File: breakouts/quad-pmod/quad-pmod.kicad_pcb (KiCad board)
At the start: 2 copper layers, 52.1 x 27.9 mm, 9 parts, among them J1 PMOD, J2 PMOD, J3 S7 Mini, J4 S7 Mini, J5 PWR, J6 PWR, J7 PMOD, J8 PMOD

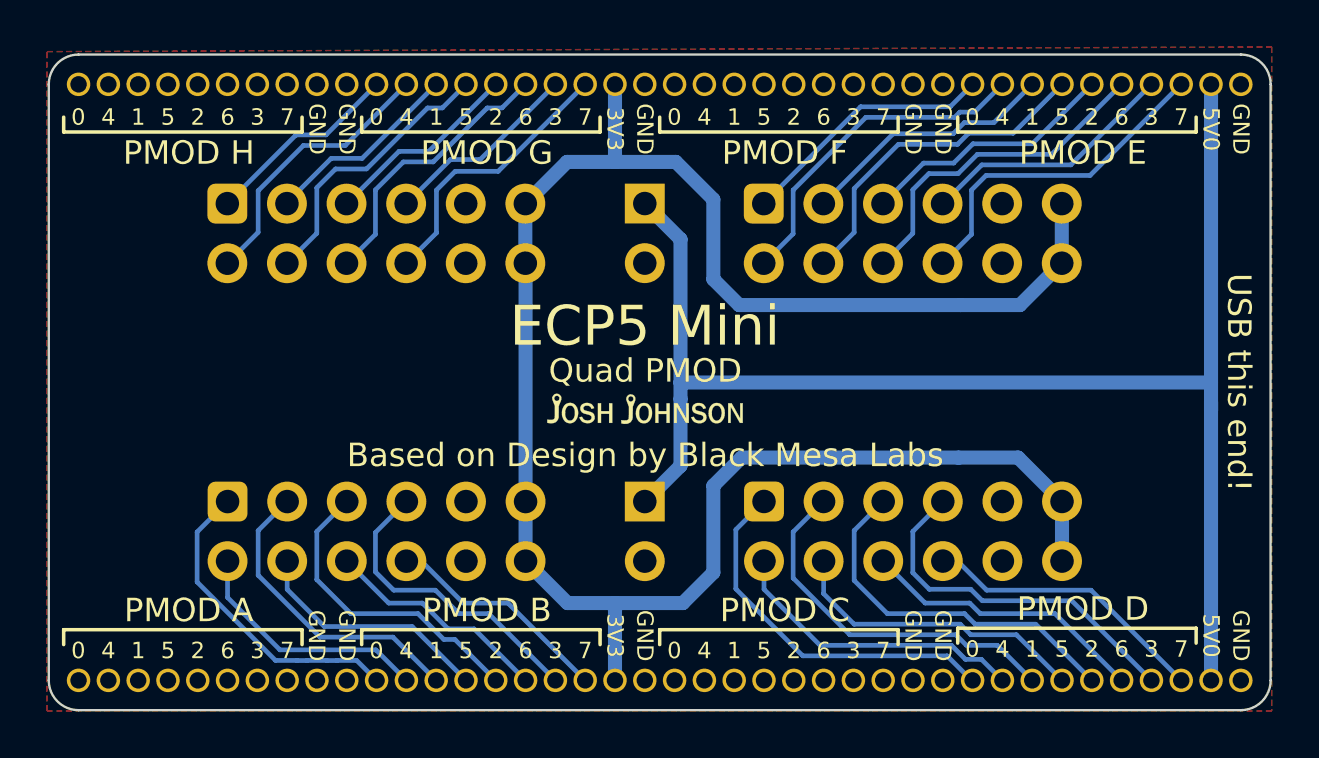
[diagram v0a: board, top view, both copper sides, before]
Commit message: update silk to clear connectors
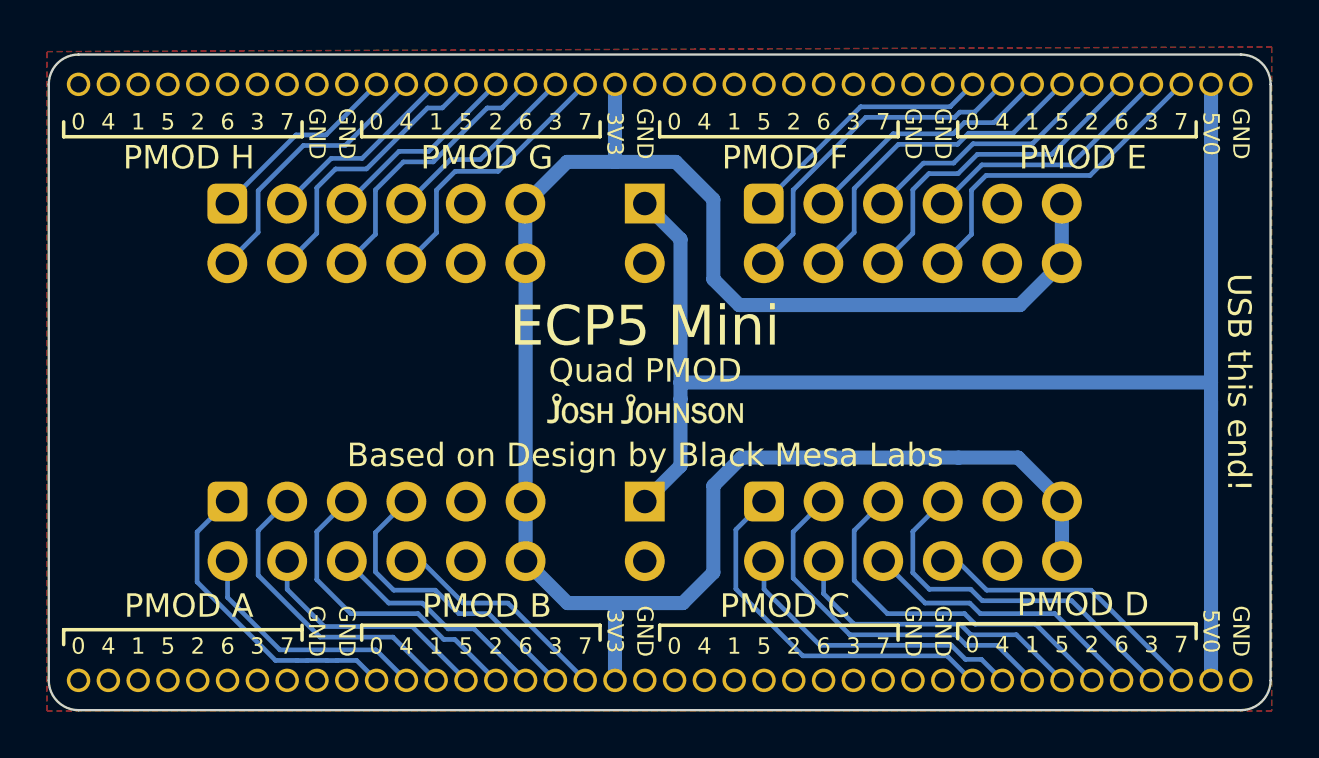
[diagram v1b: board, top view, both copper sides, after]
